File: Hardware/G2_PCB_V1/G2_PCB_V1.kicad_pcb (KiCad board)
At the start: 2 copper layers, 70 x 55 mm, 23 parts, among them P1 Ultrasonido, P2 Ultrasonido, P3 Ultrasonido, P4 EncoderDerecho, P5 EncoderIzquierdo, P6 Bateria, P7 Driver L9110, SW1 SW_Push, SW2 SW_Push, SW3 SW_Push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

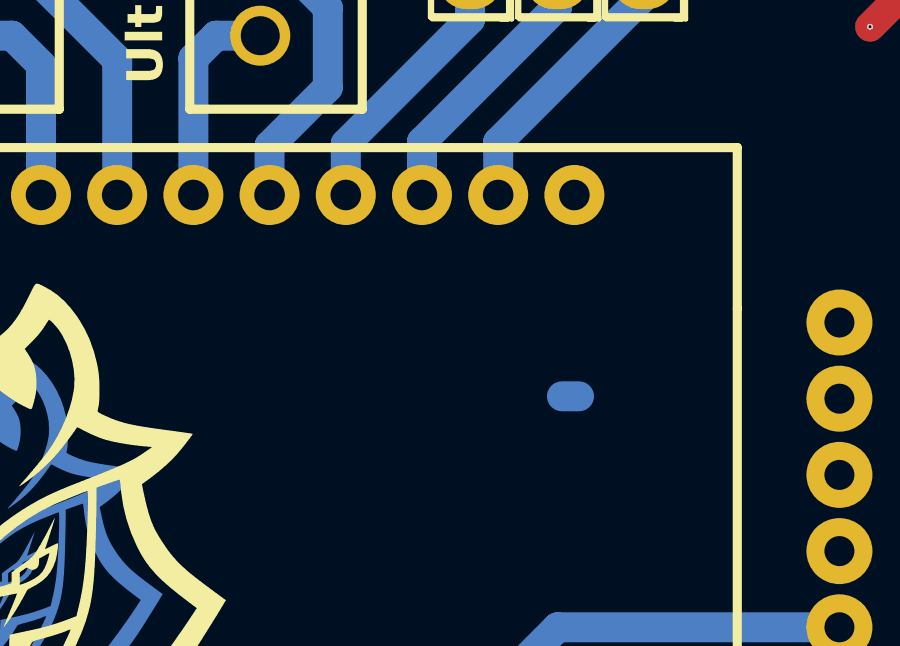
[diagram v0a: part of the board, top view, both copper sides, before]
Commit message: comence a desarrollar un modulo para la mpu9150, PCB terminado listo para fabricar y probar su funcionamiento
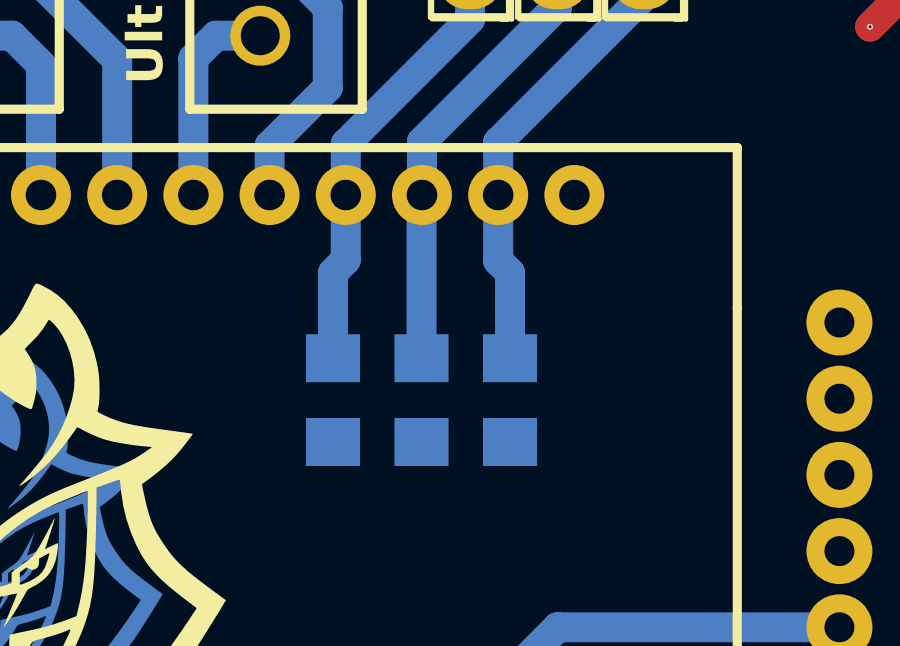
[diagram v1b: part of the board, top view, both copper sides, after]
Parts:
- added R1: 1OK, EESTN5:R_1206, B.Cu at (189.0, 83.1)
- added R2: 1OK, EESTN5:R_1206, B.Cu at (191.9, 83.1)
- added R3: 1OK, EESTN5:R_1206, B.Cu at (194.9, 83.1)
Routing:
- net /BOTON3: track 8.93 -> 14.6 mm
- net /BOTON: track 9.23 -> 14.8 mm
- net /BOTON2: track 9.09 -> 14.5 mm
- net GND: track 162.4 -> 161.8 mm
